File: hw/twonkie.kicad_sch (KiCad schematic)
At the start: 59 parts, among them J1 USB4151, J2 690-024-294T331, J3 629105150521, Q1 BSD840N, Q2 BSD840N, Q3 BSD840N, Q4 BSD840N, SW1 EVQ-P7M01P, U1 INA237, U2 INA237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

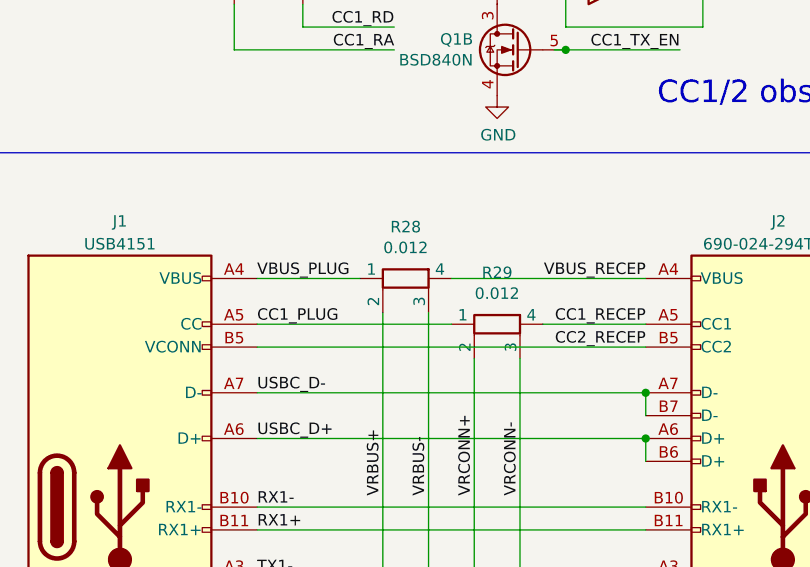
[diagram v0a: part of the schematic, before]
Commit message: v2.0: Updates based on David's review
* Wire sense resistors according to datasheet (measured current flows
  along a long edge instead of diagonally)
* Rotate R28 and move C9 to allow for that, this also unclutters the
  vias and traces around the INA237 north sides and improves copper
  plane shape
* Connect inner VBUS shape to upper via group too
* Give the RX2 pair a little more breathing room

Thanks @dnschneid for the review! <3 (see #4)
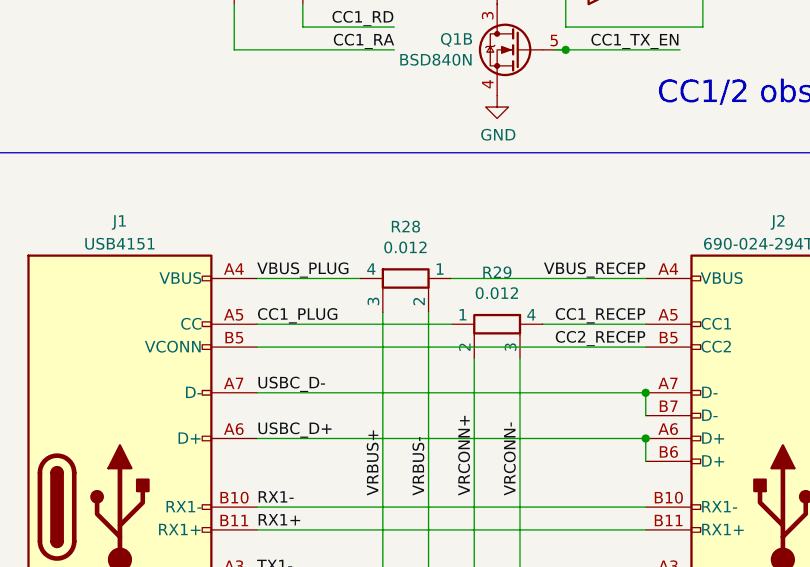
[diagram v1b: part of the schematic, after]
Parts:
- R28, R29: footprint Resistor_SMD:R_Shunt_Ohmite_LVK12 -> twonkie:R_Shunt_Ohmite_LVK12
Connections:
- net VBUS_PLUG: now also R28.4; no longer R28.1
- net VBUS_RECEP: now also R28.1; no longer R28.4
- net VRBUS+: now also R28.3; no longer R28.2
- net VRBUS-: now also R28.2; no longer R28.3
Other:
- moved on the sheet: R28
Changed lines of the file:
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@@
     (pin "1")
   )
-  (symbol (lib_id "Device:R_Shunt") (at 68.58 78.74 90) (mirror x) (unit 1)
+  (symbol (lib_id "Device:R_Shunt") (at 68.58 78.74 270) (unit 1)
     (in_bom yes) (on_board yes)
     (property "Reference" "R28" (id 0) (at 68.58 73.025 90))
     (property "Value" "0.012" (id 1) (at 68.58 75.3364 90))
-    (property "Footprint" "Resistor_SMD:R_Shunt_Ohmite_LVK12" (id 2) (at 68.58 76.962 90)
+    (property "Footprint" "twonkie:R_Shunt_Ohmite_LVK12" (id 2) (at 68.58 76.962 90)
       (effects (font (size 1.27 1.27)) hide)
     )
@@
     (property "Reference" "R29" (id 0) (at 78.74 78.105 90))
     (property "Value" "0.012" (id 1) (at 78.74 80.4164 90))
-    (property "Footprint" "Resistor_SMD:R_Shunt_Ohmite_LVK12" (id 2) (at 78.74 82.042 90)
+    (property "Footprint" "twonkie:R_Shunt_Ohmite_LVK12" (id 2) (at 78.74 82.042 90)
       (effects (font (size 1.27 1.27)) hide)
     )
@@
     )
     (path "/00000000-0000-0000-0000-000060b23623"
-      (reference "R28") (unit 1) (value "0.012") (footprint "Resistor_SMD:R_Shunt_Ohmite_LVK12")
+      (reference "R28") (unit 1) (value "0.012") (footprint "twonkie:R_Shunt_Ohmite_LVK12")
     )
     (path "/00000000-0000-0000-0000-000060d0f11c"
-      (reference "R29") (unit 1) (value "0.012") (footprint "Resistor_SMD:R_Shunt_Ohmite_LVK12")
+      (reference "R29") (unit 1) (value "0.012") (footprint "twonkie:R_Shunt_Ohmite_LVK12")
     )
     (path "/00000000-0000-0000-0000-00005ff46d11"

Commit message: Update USB-C receptacle part
The EDAC part is obsolete; use a fitting drop-in replacement from GCT.
Fixes #6.
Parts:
- J2: DigiKey P/N 151-1601-1-ND -> 2073-USB4070-30-CCT-ND; Manufacturer EDAC -> GCT; Mfg P/N 690-024-294T331 -> USB4070-30-C
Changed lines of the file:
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@@
       (effects (font (size 1.27 1.27)) hide)
     )
-    (property "DigiKey P/N" "151-1601-1-ND" (id 4) (at 110.49 104.14 0)
+    (property "DigiKey P/N" "2073-USB4070-30-CCT-ND" (id 4) (at 110.49 104.14 0)
       (effects (font (size 1.27 1.27)) hide)
     )
-    (property "Manufacturer" "EDAC" (id 5) (at 110.49 104.14 0)
+    (property "Manufacturer" "GCT" (id 5) (at 110.49 104.14 0)
       (effects (font (size 1.27 1.27)) hide)
     )
-    (property "Mfg P/N" "690-024-294T331" (id 6) (at 110.49 104.14 0)
+    (property "Mfg P/N" "USB4070-30-C" (id 6) (at 110.49 104.14 0)
       (effects (font (size 1.27 1.27)) hide)
     )

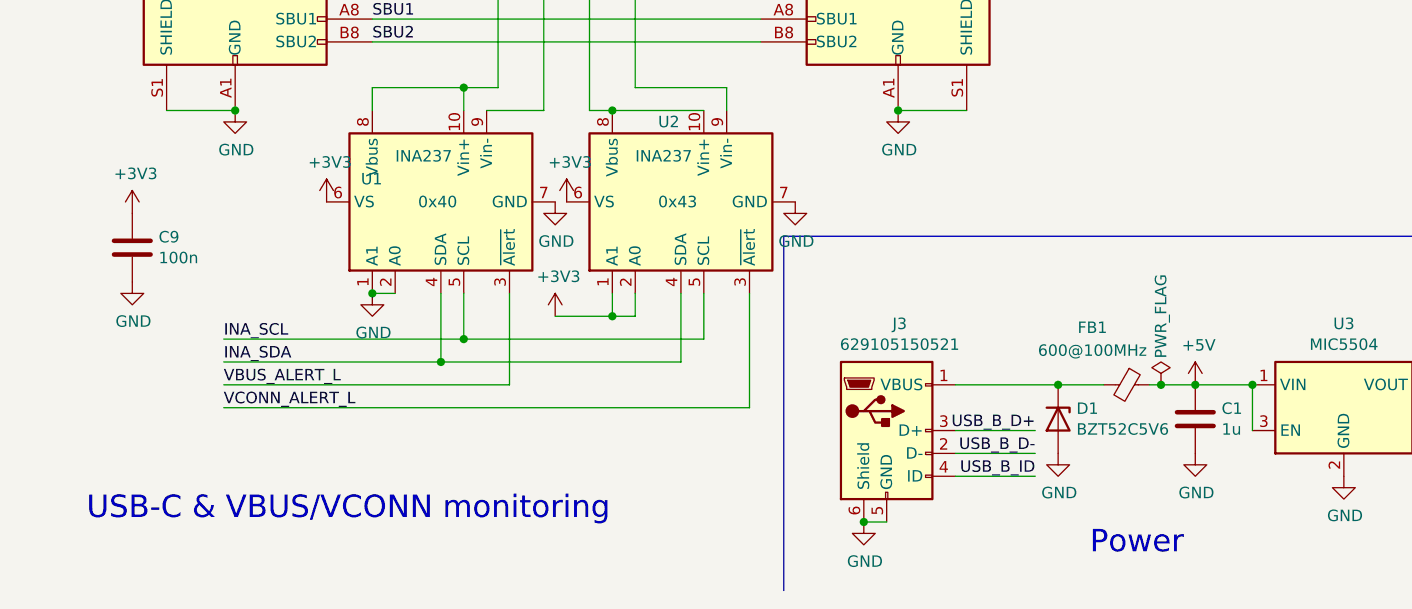
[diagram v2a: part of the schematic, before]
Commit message: hw: Update AD8606 P/N, change all caps to C_Small symbol
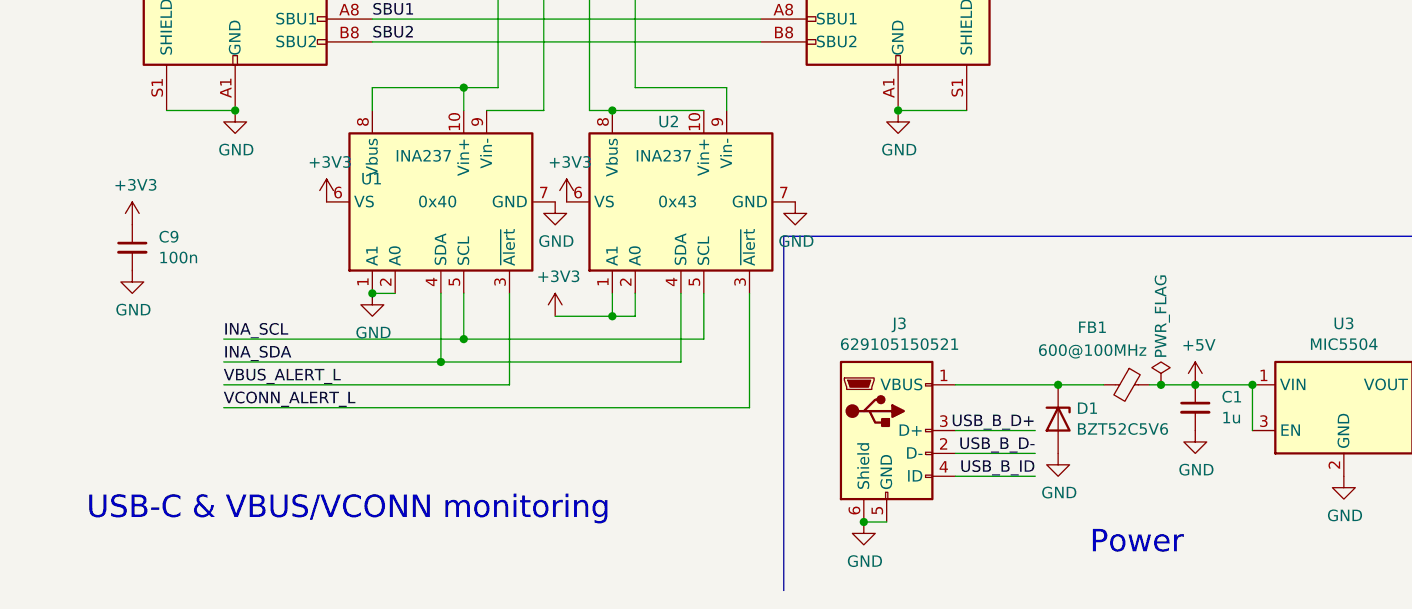
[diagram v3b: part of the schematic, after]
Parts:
- C1, C9: symbol Device:C -> Device:C_Small
- U5: DigiKey P/N AD8606ARMZREELCT-ND -> 505-AD8606ARMZ-R7CT-ND; Mfg P/N AD8606ARMZ-REEL -> AD8606ARMZ-R7
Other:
- moved on the sheet: C1
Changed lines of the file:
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@@
       (effects (font (size 1.27 1.27)) hide)
     )
-    (property "DigiKey P/N" "AD8606ARMZREELCT-ND" (id 4) (at 93.98 43.18 0)
+    (property "DigiKey P/N" "505-AD8606ARMZ-R7CT-ND" (id 4) (at 93.98 43.18 0)
       (effects (font (size 1.27 1.27)) hide)
     )
@@
       (effects (font (size 1.27 1.27)) hide)
     )
-    (property "Mfg P/N" "AD8606ARMZ-REEL" (id 6) (at 93.98 43.18 0)
+    (property "Mfg P/N" "AD8606ARMZ-R7" (id 6) (at 93.98 43.18 0)
       (effects (font (size 1.27 1.27)) hide)
     )
@@
     (pin "2")
   )
-  (symbol (lib_id "Device:C") (at 143.51 179.07 0) (unit 1)
-    (in_bom yes) (on_board yes)
-    (property "Reference" "C1" (id 0) (at 146.431 177.9016 0)
-      (effects (font (size 1.27 1.27)) (justify left))
-    )
-    (property "Value" "1u" (id 1) (at 146.431 180.213 0)
-      (effects (font (size 1.27 1.27)) (justify left))
-    )
-    (property "Footprint" "Capacitor_SMD:C_0402_1005Metric_Pad0.74x0.62mm_HandSolder" (id 2) (at 144.4752 182.88 0)
-      (effects (font (size 1.27 1.27)) hide)
-    )
-    (property "Datasheet" "~" (id 3) (at 143.51 179.07 0)
-      (effects (font (size 1.27 1.27)) hide)
-    )
-    (property "DigiKey P/N" "1276-1235-1-ND" (id 4) (at 143.51 179.07 0)
-      (effects (font (size 1.27 1.27)) hide)
-    )
-    (property "Manufacturer" "Samsung Electro-Mechanics" (id 5) (at 143.51 179.07 0)
-      (effects (font (size 1.27 1.27)) hide)
-    )
-    (property "Mfg P/N" "CL05A105MQ5NNNC" (id 6) (at 143.51 179.07 0)
+  (symbol (lib_id "Device:C_Small") (at 143.51 177.8 0) (unit 1)
+    (in_bom yes) (on_board yes)
+    (property "Reference" "C1" (id 0) (at 146.431 176.6316 0)
+      (effects (font (size 1.27 1.27)) (justify left))
+    )
+    (property "Value" "1u" (id 1) (at 146.431 178.943 0)
+      (effects (font (size 1.27 1.27)) (justify left))
+    )
+    (property "Footprint" "Capacitor_SMD:C_0402_1005Metric_Pad0.74x0.62mm_HandSolder" (id 2) (at 143.51 177.8 0)
+      (effects (font (size 1.27 1.27)) hide)
+    )
+    (property "Datasheet" "~" (id 3) (at 143.51 177.8 0)
+      (effects (font (size 1.27 1.27)) hide)
+    )
+    (property "DigiKey P/N" "1276-1235-1-ND" (id 4) (at 143.51 177.8 0)
+      (effects (font (size 1.27 1.27)) hide)
+    )
+    (property "Manufacturer" "Samsung Electro-Mechanics" (id 5) (at 143.51 177.8 0)
+      (effects (font (size 1.27 1.27)) hide)
+    )
+    (property "Mfg P/N" "CL05A105MQ5NNNC" (id 6) (at 143.51 177.8 0)
       (effects (font (size 1.27 1.27)) hide)
     )
@@
     (pin "1")
   )
-  (symbol (lib_id "power:GND") (at 143.51 182.88 0) (unit 1)
-    (in_bom yes) (on_board yes)
-    (property "Reference" "#PWR0111" (id 0) (at 143.51 189.23 0)
-      (effects (font (size 1.27 1.27)) hide)
-    )
-    (property "Value" "GND" (id 1) (at 143.637 187.2742 0))
-    (property "Footprint" "" (id 2) (at 143.51 182.88 0)
-      (effects (font (size 1.27 1.27)) hide)
-    )
-    (property "Datasheet" "" (id 3) (at 143.51 182.88 0)
+  (symbol (lib_id "power:GND") (at 143.51 180.34 0) (unit 1)
+    (in_bom yes) (on_board yes)
+    (property "Reference" "#PWR0111" (id 0) (at 143.51 186.69 0)
+      (effects (font (size 1.27 1.27)) hide)
+    )
+    (property "Value" "GND" (id 1) (at 143.637 184.7342 0))
+    (property "Footprint" "" (id 2) (at 143.51 180.34 0)
+      (effects (font (size 1.27 1.27)) hide)
+    )
+    (property "Datasheet" "" (id 3) (at 143.51 180.34 0)
       (effects (font (size 1.27 1.27)) hide)
     )
@@
       (effects (font (size 1.27 1.27)) hide)
     )
-    (property "DigiKey P/N" "AD8606ARMZREELCT-ND" (id 4) (at 193.04 43.18 0)
+    (property "DigiKey P/N" "505-AD8606ARMZ-R7CT-ND" (id 4) (at 193.04 43.18 0)
       (effects (font (size 1.27 1.27)) hide)
     )
@@
       (effects (font (size 1.27 1.27)) hide)
     )
-    (property "Mfg P/N" "AD8606ARMZ-REEL" (id 6) (at 193.04 43.18 0)
+    (property "Mfg P/N" "AD8606ARMZ-R7" (id 6) (at 193.04 43.18 0)
       (effects (font (size 1.27 1.27)) hide)
     )
@@
       (effects (font (size 1.27 1.27)) hide)
     )
-    (property "DigiKey P/N" "AD8606ARMZREELCT-ND" (id 4) (at 111.76 21.59 0)
+    (property "DigiKey P/N" "505-AD8606ARMZ-R7CT-ND" (id 4) (at 111.76 21.59 0)
       (effects (font (size 1.27 1.27)) hide)
     )
@@
       (effects (font (size 1.27 1.27)) hide)
     )
-    (property "Mfg P/N" "AD8606ARMZ-REEL" (id 6) (at 111.76 21.59 0)
+    (property "Mfg P/N" "AD8606ARMZ-R7" (id 6) (at 111.76 21.59 0)
       (effects (font (size 1.27 1.27)) hide)
     )
@@
     (pin "1")
   )
-  (symbol (lib_id "Device:C") (at 25.4 160.02 0) (unit 1)
+  (symbol (lib_id "Device:C_Small") (at 25.4 160.02 0) (unit 1)
     (in_bom yes) (on_board yes)
     (property "Reference" "C9" (id 0) (at 28.321 158.8516 0)
@@
       (effects (font (size 1.27 1.27)) (justify left))
     )
-    (property "Footprint" "Capacitor_SMD:C_0402_1005Metric_Pad0.74x0.62mm_HandSolder" (id 2) (at 26.3652 163.83 0)
+    (property "Footprint" "Capacitor_SMD:C_0402_1005Metric_Pad0.74x0.62mm_HandSolder" (id 2) (at 25.4 160.02 0)
       (effects (font (size 1.27 1.27)) hide)
     )
@@
     (pin "2")
   )
-  (symbol (lib_id "power:GND") (at 25.4 163.83 0) (unit 1)
-    (in_bom yes) (on_board yes)
-    (property "Reference" "#PWR02" (id 0) (at 25.4 170.18 0)
-      (effects (font (size 1.27 1.27)) hide)
-    )
-    (property "Value" "GND" (id 1) (at 25.527 168.2242 0))
-    (property "Footprint" "" (id 2) (at 25.4 163.83 0)
-      (effects (font (size 1.27 1.27)) hide)
-    )
-    (property "Datasheet" "" (id 3) (at 25.4 163.83 0)
-      (effects (font (size 1.27 1.27)) hide)
-    )
-    (pin "1")
-  )
-  (symbol (lib_id "power:+3V3") (at 25.4 156.21 0) (unit 1)
-    (in_bom yes) (on_board yes)
-    (property "Reference" "#PWR01" (id 0) (at 25.4 160.02 0)
-      (effects (font (size 1.27 1.27)) hide)
-    )
-    (property "Value" "+3V3" (id 1) (at 25.781 151.8158 0))
-    (property "Footprint" "" (id 2) (at 25.4 156.21 0)
-      (effects (font (size 1.27 1.27)) hide)
-    )
-    (property "Datasheet" "" (id 3) (at 25.4 156.21 0)
-      (effects (font (size 1.27 1.27)) hide)
-    )
+  (symbol (lib_id "power:GND") (at 25.4 162.56 0) (unit 1)
+    (in_bom yes) (on_board yes)
+    (property "Reference" "#PWR02" (id 0) (at 25.4 168.91 0)
+      (effects (font (size 1.27 1.27)) hide)
+    )
+    (property "Value" "GND" (id 1) (at 25.527 166.9542 0))
+    (property "Footprint" "" (id 2) (at 25.4 162.56 0)
+      (effects (font (size 1.27 1.27)) hide)
+    )
+    (property "Datasheet" "" (id 3) (at 25.4 162.56 0)
+      (effects (font (size 1.27 1.27)) hide)
+    )
+    (pin "1")
+  )
+  (symbol (lib_id "power:+3V3") (at 25.4 157.48 0) (unit 1)
+    (in_bom yes) (on_board yes)
+    (property "Reference" "#PWR01" (id 0) (at 25.4 161.29 0)
+      (effects (font (size 1.27 1.27)) hide)
+    )
+    (property "Value" "+3V3" (id 1) (at 25.781 153.0858 0))
+    (property "Footprint" "" (id 2) (at 25.4 157.48 0)
+      (effects (font (size 1.27 1.27)) hide)
+    )
+    (property "Datasheet" "" (id 3) (at 25.4 157.48 0)
+      (effects (font (size 1.27 1.27)) hide)
+    )

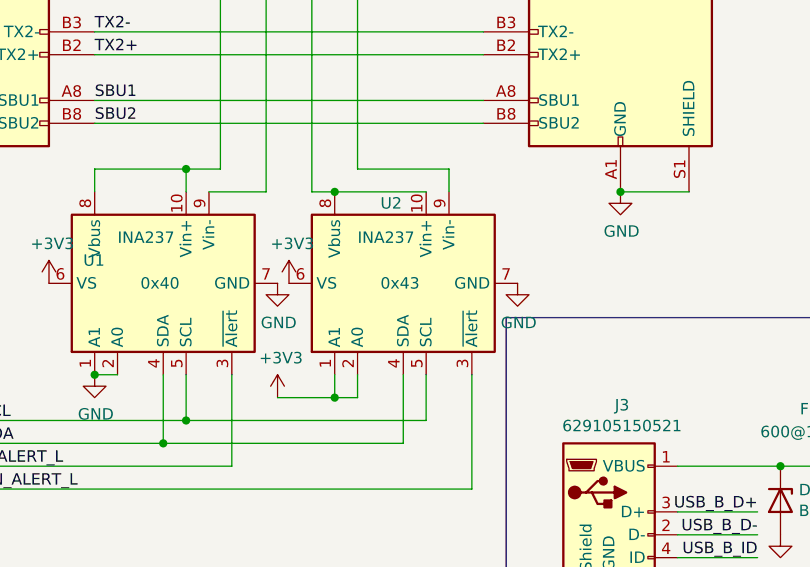
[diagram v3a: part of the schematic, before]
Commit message: Fix VCONN INA I2C address in schematic
Just a typo - board and firmware are fine.

Fixes #11
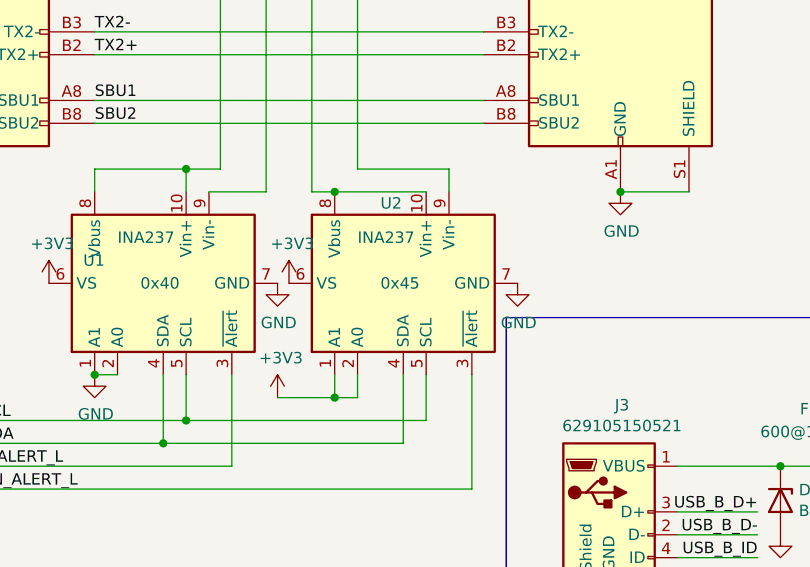
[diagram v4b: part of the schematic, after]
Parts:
- U2: I2C addr 0x43 -> 0x45
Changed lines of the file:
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@@
       (effects (font (size 1.27 1.27)) hide)
     )
-    (property "I2C addr" "0x43" (id 4) (at 83.82 154.94 90)
+    (property "I2C addr" "0x45" (id 4) (at 83.82 154.94 90)
       (effects (font (size 1.27 1.27)) (justify right))
     )
